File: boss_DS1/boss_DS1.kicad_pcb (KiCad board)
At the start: 2 copper layers, 80 x 100 mm, 84 parts, among them J1 top_panel_connector, J2 Jack_6.35, J6 Jack_6.35, J7 Conn_01x01_Socket, J8 Conn_01x01_Socket, J9 Barrel_Jack_Switch, P1 boss_DS1_front_panel, P2 bottom_panel, Q1 MMBT5551, Q11 AO3401A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

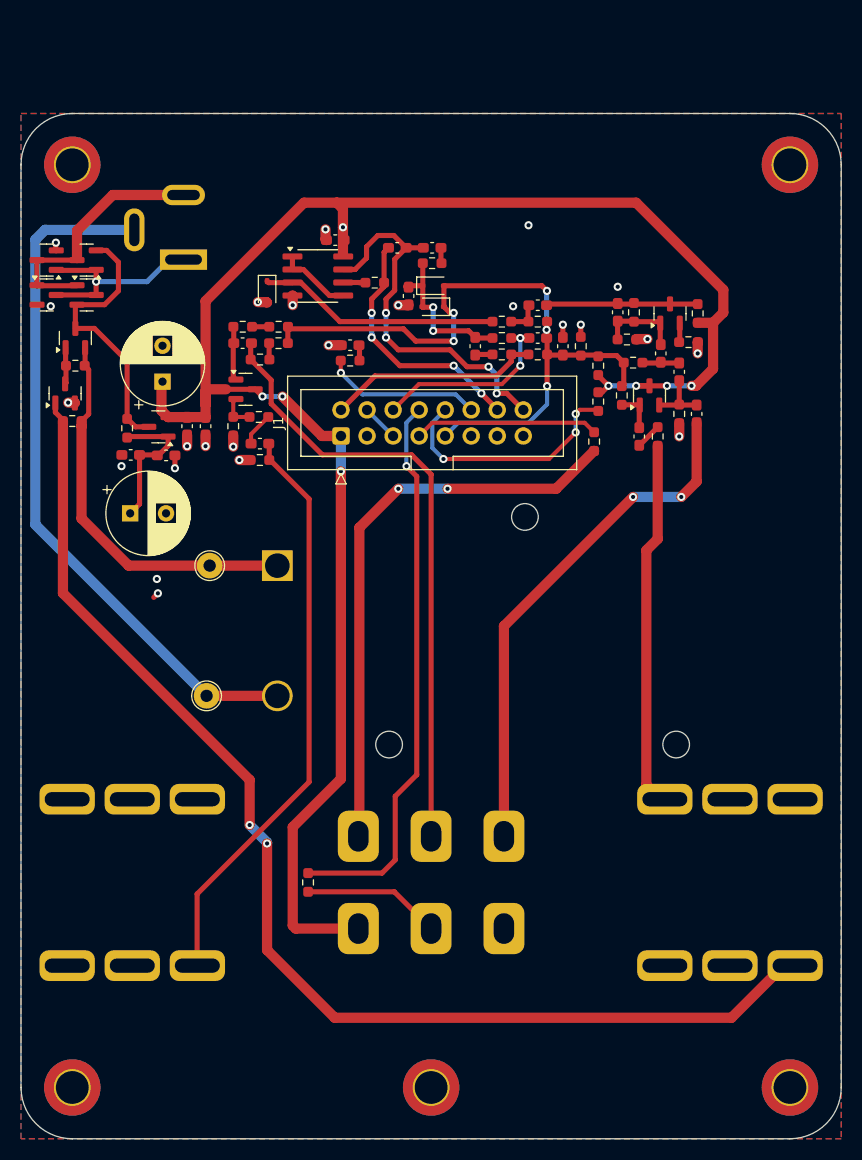
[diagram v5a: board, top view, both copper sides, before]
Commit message: Rounded traces.
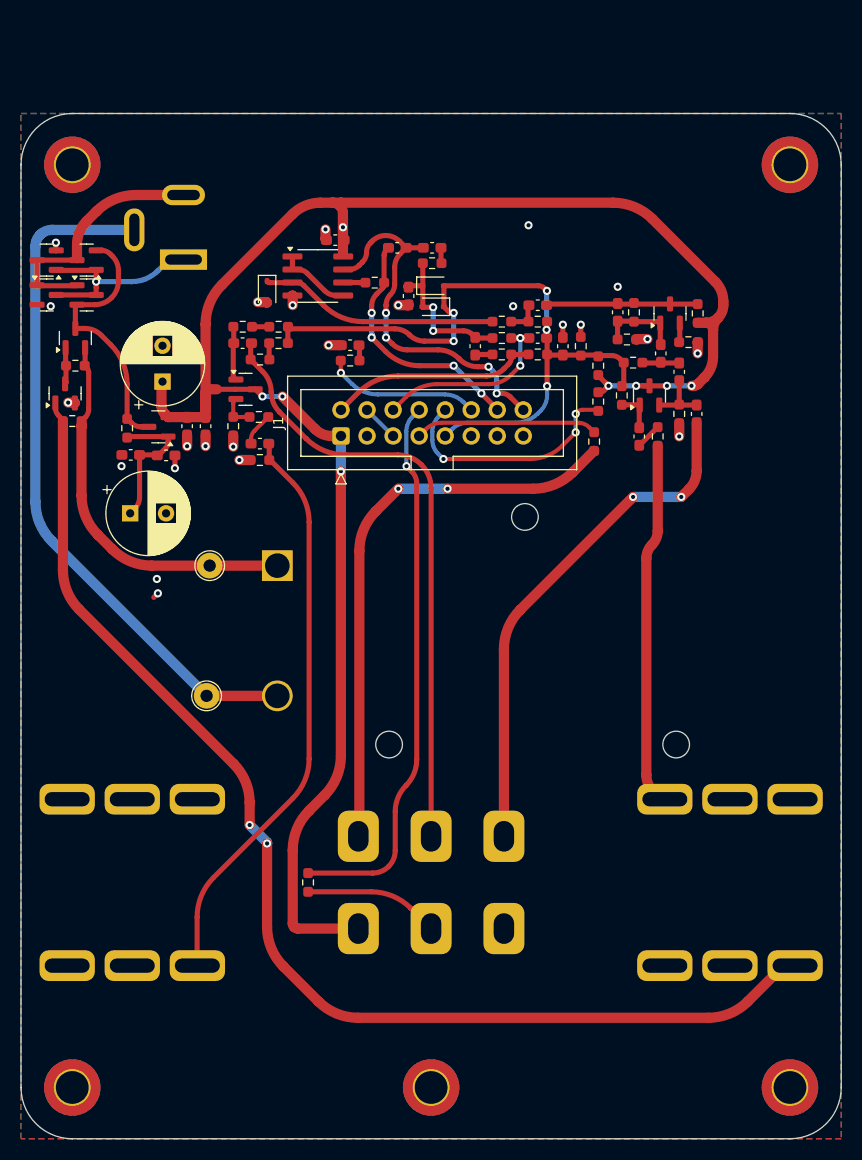
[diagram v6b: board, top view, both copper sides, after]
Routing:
- net IN_CONNECT: track 118.3 -> 116.9 mm
- net Net-(J1C-Pin_16): track 37.3 -> 36.2 mm
- net /SW_MID: track 62.4 -> 61.6 mm
- net REG_IN: track 26.9 -> 26.0 mm
- net /SW_ON: track 56.0 -> 55.2 mm
- net /OUTPUT: track 57.1 -> 56.3 mm
- net Net-(J1D-Pin_8): track 54.7 -> 54.0 mm
- net BAT+: track 38.3 -> 37.6 mm
- net 4V5: track 68.1 -> 67.5 mm

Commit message: Ready for production.
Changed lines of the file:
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@@
 			(outputformat 1)
 			(mirror no)
-			(drillshape 1)
+			(drillshape 0)
 			(scaleselection 1)
-			(outputdirectory "")
+			(outputdirectory "gerbers/")
 		)
 	)
@@
 			(at 1.27 -6.1 90)
 			(layer "F.SilkS")
+			(hide yes)
 			(effects
 				(font
